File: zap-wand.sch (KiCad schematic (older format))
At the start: 14 parts

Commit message: Various bits
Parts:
- removed C?: 100u, symbol C
- removed Q? (x2): Q_NPN_EBC, symbol Q_NPN_EBC
- removed Q?: Q_NMOS_GDS, symbol Q_NMOS_GDS
- removed R?: 510R, symbol R
- removed R? (x2): 1k, symbol R
- removed R?: 100k, symbol R
- removed SW_PWR: SWITCH_SPST, symbol SWITCH_SPST
- added C2: 47u, agg:0805, symbol C
- added C3, C4: 1u, agg:0805, symbol C_Small
- added IC1: NC7WZ02, agg-dev:US8-3.1mm, symbol NC7WZ02
- added Q1: Q_PMOS_GDS, agg:SOT-323, symbol Q_PMOS_GDS
- added R1: 1k, agg:0805, symbol R
- added R2: 100k, agg:0805, symbol R
- added RV1: 100k, parts:PVZ2A, symbol POT
- added U1: NCP103, parts:UDFN4, symbol NCP103
- BATT1: renamed from BATT; footprint (none) -> agg:SM02B-PASS
- C1: renamed from C?; footprint (none) -> agg:0805; Farnell (none) -> 2497051
- D1: renamed from D?; footprint (none) -> LEDs:LED-5MM
- R3: renamed from R?; value 1k -> 100R; footprint (none) -> agg:0805; Farnell (none) -> 2447552
- SW1: renamed from SW?; footprint (none) -> parts:FSM10JH; Farnell (none) -> 1555986
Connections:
- net labels added: +3V3, GND
- wire segments 13 -> 17
- no-connect marks 0 -> 1

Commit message: Various tweaks and fixes
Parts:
- removed RV1: 100k, parts:PVZ2A, symbol POT
- added R4: 10k, agg:0603, symbol R
- added R5: 18k, agg:0603, symbol R
- BATT1: footprint agg:SM02B-PASS -> agg:SIL-254P-02
- C1: footprint agg:0805 -> agg:0603; Farnell 2497051 -> 2494233
- C2: value 47u -> 10n; Farnell 2362109 -> 2470490
- C3, C4: footprint agg:0805 -> agg:0603; Farnell 2496995 -> 2362099
- D1: footprint LEDs:LED-5MM -> agg:SIL-254P-02
- R1: footprint agg:0805 -> agg:0603; Farnell 2447473 -> 9330380
- R2: value 100k -> 820k; footprint agg:0805 -> agg:0603; Farnell 2447551 -> 9331581
- R3: footprint agg:0805 -> agg:0603; Farnell 2447552 -> 2447227
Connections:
- net +3V3: now also R5.1; no longer R2.1
- net GND: now also R4.1
- net at C1.2, SW1.2: now also R4.2
- net at C2.1, IC1.5 (A2), IC1.6 (B2): now also R2.2
- new net: R2.1, R5.2
- no-connect marks 1 -> 0
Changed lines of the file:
@@
 F 0 "BATT1" H 1218 2075 50  0001 L CNN
 F 1 "Battery" H 1218 2030 50  0001 L CNN
-F 2 "agg:SM02B-PASS" V 1100 2115 50  0001 C CNN
+F 2 "agg:SIL-254P-02" V 1100 2115 50  0001 C CNN
 F 3 "" V 1100 2115 50  0000 C CNN
 	1    1100 2075
@@
 F 0 "D1" H 5096 2442 50  0001 R CNN
 F 1 "LED" V 5050 2442 50  0001 R CNN
-F 2 "LEDs:LED-5MM" H 5050 2550 50  0001 C CNN
+F 2 "agg:SIL-254P-02" H 5050 2550 50  0001 C CNN
 F 3 "" H 5050 2550 50  0000 C CNN
 	1    5050 2550
@@
 F 0 "R3" H 4980 2154 50  0001 R CNN
 F 1 "100R" V 5050 2200 50  0000 C CNN
-F 2 "agg:0805" V 4980 2200 50  0001 C CNN
-F 3 "http://www.farnell.com/datasheets/1849611.pdf?_ga=1.16398518.1253160071.1453215511" H 5050 2200 50  0001 C CNN
-F 4 "2447552" H 5050 2200 60  0001 C CNN "Farnell"
+F 2 "agg:0603" V 4980 2200 50  0001 C CNN
+F 3 "http://www.farnell.com/datasheets/1849611.pdf?_ga=1.214886046.860814275.1465901405" H 5050 2200 50  0001 C CNN
+F 4 "2447227" H 5050 2200 60  0001 C CNN "Farnell"
 	1    5050 2200
 	-1   0    0    1
@@
 F 0 "C1" V 2873 1800 50  0001 C CNN
 F 1 "10u" V 2965 1800 50  0000 C CNN
-F 2 "agg:0805" H 3163 1650 50  0001 C CNN
-F 3 "http://www.farnell.com/datasheets/1958513.pdf?_ga=1.212596244.1253160071.1453215511" H 3125 1800 50  0001 C CNN
-F 4 "2497051" H 3125 1800 60  0001 C CNN "Farnell"
+F 2 "agg:0603" H 3163 1650 50  0001 C CNN
+F 3 "http://www.farnell.com/datasheets/1955682.pdf?_ga=1.157737651.860814275.1465901405" H 3125 1800 50  0001 C CNN
+F 4 "2494233" H 3125 1800 60  0001 C CNN "Farnell"
 	1    3125 1800
 	0    1    1    0
@@
 P 4025 1850
 F 0 "C2" V 3773 1850 50  0001 C CNN
-F 1 "47u" V 3865 1850 50  0000 C CNN
+F 1 "10n" V 3865 1850 50  0000 C CNN
 F 2 "agg:0805" H 4063 1700 50  0001 C CNN
-F 3 "http://www.farnell.com/datasheets/2047835.pdf" H 4025 1850 50  0001 C CNN
-F 4 "2362109" H 4025 1850 60  0001 C CNN "Farnell"
+F 3 "http://www.farnell.com/datasheets/1889704.pdf?_ga=1.190770722.860814275.1465901405" H 4025 1850 50  0001 C CNN
+F 4 "2470490" H 4025 1850 60  0001 C CNN "Farnell"
 	1    4025 1850
 	0    1    1    0
@@
 F 0 "R1" H 3205 1904 50  0001 R CNN
 F 1 "1k" V 3275 1950 50  0000 C CNN
-F 2 "agg:0805" V 3205 1950 50  0001 C CNN
-F 3 "http://www.farnell.com/datasheets/1849611.pdf?_ga=1.167509182.1253160071.1453215511" H 3275 1950 50  0001 C CNN
-F 4 "2447473" H 3275 1950 60  0001 C CNN "Farnell"
+F 2 "agg:0603" V 3205 1950 50  0001 C CNN
+F 3 "http://www.farnell.com/datasheets/1788326.pdf?_ga=1.214886046.860814275.1465901405" H 3275 1950 50  0001 C CNN
+F 4 "9330380" H 3275 1950 60  0001 C CNN "Farnell"
 	1    3275 1950
 	-1   0    0    1
@@
 Connection ~ 4750 1850
 $Comp
-L GND #PWR09
+L GND #PWR05
 U 1 1 578BBB74
 P 2200 2250
-F 0 "#PWR09" H 2200 2000 50  0001 C CNN
+F 0 "#PWR05" H 2200 2000 50  0001 C CNN
 F 1 "GND" H 2325 2175 50  0001 C CNN
 F 2 "" H 2200 2250 50  0000 C CNN
@@
 	1    0    0    -1
 $EndComp
-$Comp
-L POT RV1
-U 1 1 578BD570
-P 4175 1600
-F 0 "RV1" H 4175 1386 50  0001 C CNN
-F 1 "100k" H 4175 1600 50  0000 C CNN
-F 2 "parts:PVZ2A" H 4175 1600 50  0001 C CNN
-F 3 "http://www.farnell.com/datasheets/477473.pdf?_ga=1.242785154.1253160071.1453215511" H 4175 1600 50  0001 C CNN
-F 4 "1771728" H 4175 1600 60  0001 C CNN "Farnell"
-	1    4175 1600
-	1    0    0    1
-$EndComp
 Wire Wire Line
 	4175 1850 4175 1750
-NoConn ~ 4325 1600
 $Comp
 L R R2
 U 1 1 578BDA2A
-P 3875 1600
-F 0 "R2" H 3805 1554 50  0001 R CNN
-F 1 "100k" V 3875 1600 50  0000 C CNN
-F 2 "agg:0805" V 3805 1600 50  0001 C CNN
-F 3 "http://www.farnell.com/datasheets/1849611.pdf?_ga=1.167509182.1253160071.1453215511" H 3875 1600 50  0001 C CNN
-F 4 "2447551" H 3875 1600 60  0001 C CNN "Farnell"
-	1    3875 1600
-	0    -1   -1   0
+P 4175 1600
+F 0 "R2" H 4105 1554 50  0001 R CNN
+F 1 "820k" V 4175 1600 50  0000 C CNN
+F 2 "agg:0603" V 4105 1600 50  0001 C CNN
+F 3 "http://www.farnell.com/datasheets/1788326.pdf?_ga=1.148300478.860814275.1465901405" H 4175 1600 50  0001 C CNN
+F 4 "9331581" H 4175 1600 60  0001 C CNN "Farnell"
+	1    4175 1600
+	1    0    0    -1
 $EndComp
 $Comp
@@
 	1100 2250 2200 2250
 Connection ~ 1400 2100
-$Comp
-L C_Small C4
-U 1 1 578C05A9
-P 2200 2100
-F 0 "C4" H 2292 2146 50  0001 L CNN
-F 1 "1u" H 2300 2100 50  0000 L CNN
-F 2 "agg:0805" H 2200 2100 50  0001 C CNN
-F 3 "http://www.farnell.com/datasheets/1958513.pdf?_ga=1.205166480.1253160071.1453215511" H 2200 2100 50  0001 C CNN
-F 4 "2496995" H 2200 2100 60  0001 C CNN "Farnell"
-	1    2200 2100
-	1    0    0    -1
-$EndComp
 Connection ~ 1400 2250
 Wire Wire Line
@@
 P 1400 2000
 F 0 "C3" H 1492 2046 50  0001 L CNN
-F 1 "1u" H 1250 2000 50  0000 L CNN
-F 2 "agg:0805" H 1400 2000 50  0001 C CNN
-F 3 "http://www.farnell.com/datasheets/1958513.pdf?_ga=1.205166480.1253160071.1453215511" H 1400 2000 50  0001 C CNN
-F 4 "2496995" H 1400 2000 60  0001 C CNN "Farnell"
+F 1 "1u" H 1475 2000 50  0000 L CNN
+F 2 "agg:0603" H 1400 2000 50  0001 C CNN
+F 3 "http://www.farnell.com/datasheets/2047881.pdf?_ga=1.124134275.860814275.1465901405" H 1400 2000 50  0001 C CNN
+F 4 "2362099" H 1400 2000 60  0001 C CNN "Farnell"
 	1    1400 2000
 	1    0    0    -1
 $EndComp
 $Comp
-L +3V3 #PWR?
+L +3V3 #PWR06
 U 1 1 578CFCA7
 P 2200 2000
-F 0 "#PWR?" H 2200 1850 50  0001 C CNN
+F 0 "#PWR06" H 2200 1850 50  0001 C CNN
 F 1 "+3V3" H 2215 2173 50  0000 C CNN
 F 2 "" H 2200 2000 50  0000 C CNN
@@
 $EndComp
 $Comp
-L +3V3 #PWR?
+L +3V3 #PWR07
 U 1 1 578CFCC6
 P 2775 1600
-F 0 "#PWR?" H 2775 1450 50  0001 C CNN
+F 0 "#PWR07" H 2775 1450 50  0001 C CNN
 F 1 "+3V3" H 2790 1773 50  0000 C CNN
 F 2 "" H 2775 1600 50  0000 C CNN
@@
 $EndComp
 $Comp
-L +3V3 #PWR?
+L +3V3 #PWR08
 U 1 1 578CFCE3
 P 3575 1650
-F 0 "#PWR?" H 3575 1500 50  0001 C CNN
+F 0 "#PWR08" H 3575 1500 50  0001 C CNN
 F 1 "+3V3" H 3590 1823 50  0000 C CNN
 F 2 "" H 3575 1650 50  0000 C CNN
@@
 $EndComp
 $Comp
-L +3V3 #PWR?
+L +3V3 #PWR09
 U 1 1 578CFCF1
-P 3725 1600
-F 0 "#PWR?" H 3725 1450 50  0001 C CNN
-F 1 "+3V3" H 3800 1725 50  0000 C CNN
-F 2 "" H 3725 1600 50  0000 C CNN
-F 3 "" H 3725 1600 50  0000 C CNN
-	1    3725 1600
-	1    0    0    -1
-$EndComp
-$Comp
-L +3V3 #PWR?
+P 4175 1150
+F 0 "#PWR09" H 4175 1000 50  0001 C CNN
+F 1 "+3V3" H 4250 1275 50  0000 C CNN
+F 2 "" H 4175 1150 50  0000 C CNN
+F 3 "" H 4175 1150 50  0000 C CNN
+	1    4175 1150
+	1    0    0    -1
+$EndComp
+$Comp
+L +3V3 #PWR010
 U 1 1 578CFCFF
 P 4450 1650
-F 0 "#PWR?" H 4450 1500 50  0001 C CNN
+F 0 "#PWR010" H 4450 1500 50  0001 C CNN
 F 1 "+3V3" H 4465 1823 50  0000 C CNN
 F 2 "" H 4450 1650 50  0000 C CNN
@@
 $EndComp
 $Comp
-L +3V3 #PWR?
+L +3V3 #PWR011
 U 1 1 578CFD0D
 P 5050 1650
-F 0 "#PWR?" H 5050 1500 50  0001 C CNN
+F 0 "#PWR011" H 5050 1500 50  0001 C CNN
 F 1 "+3V3" H 5065 1823 50  0000 C CNN
 F 2 "" H 5050 1650 50  0000 C CNN
@@
 	1    0    0    -1
 $EndComp
+$Comp
+L R R4
+U 1 1 578E3B6A
+P 2975 1950
+F 0 "R4" H 2905 1904 50  0001 R CNN
+F 1 "10k" V 2975 1950 50  0000 C CNN
+F 2 "agg:0603" V 2905 1950 50  0001 C CNN
+F 3 "http://www.farnell.com/datasheets/1788326.pdf?_ga=1.190834594.860814275.1465901405" H 2975 1950 50  0001 C CNN
+F 4 "9330399" H 2975 1950 60  0001 C CNN "Farnell"
+	1    2975 1950
+	-1   0    0    1
+$EndComp
+Connection ~ 2975 1800
+$Comp
+L GND #PWR012
+U 1 1 578E3BBA
+P 2975 2100
+F 0 "#PWR012" H 2975 1850 50  0001 C CNN
+F 1 "GND" H 3100 2025 50  0001 C CNN
+F 2 "" H 2975 2100 50  0000 C CNN
+F 3 "" H 2975 2100 50  0000 C CNN
+	1    2975 2100
+	1    0    0    -1
+$EndComp
+$Comp
+L R R5
+U 1 1 578E56B2
+P 4175 1300
+F 0 "R5" H 4105 1254 50  0001 R CNN
+F 1 "18k" V 4175 1300 50  0000 C CNN
+F 2 "agg:0603" V 4105 1300 50  0001 C CNN
+F 3 "http://www.farnell.com/datasheets/1788326.pdf?_ga=1.190834594.860814275.1465901405" H 4175 1300 50  0001 C CNN
+F 4 "9330720" H 4175 1300 60  0001 C CNN "Farnell"
+	1    4175 1300
+	1    0    0    -1
+$EndComp
+$Comp
+L C_Small C4
+U 1 1 578E5A07
+P 2200 2100
+F 0 "C4" H 2292 2146 50  0001 L CNN
+F 1 "1u" H 2275 2100 50  0000 L CNN
+F 2 "agg:0603" H 2200 2100 50  0001 C CNN
+F 3 "http://www.farnell.com/datasheets/2047881.pdf?_ga=1.124134275.860814275.1465901405" H 2200 2100 50  0001 C CNN
+F 4 "2362099" H 2200 2100 60  0001 C CNN "Farnell"
+	1    2200 2100
+	1    0    0    -1
+$EndComp

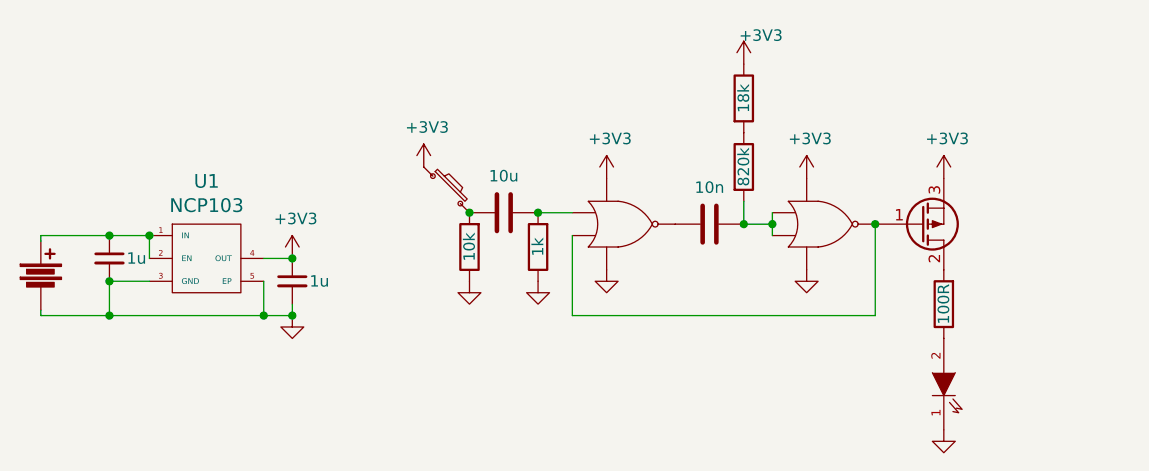
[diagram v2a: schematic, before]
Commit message: Beefier regulator, pcb shuffle
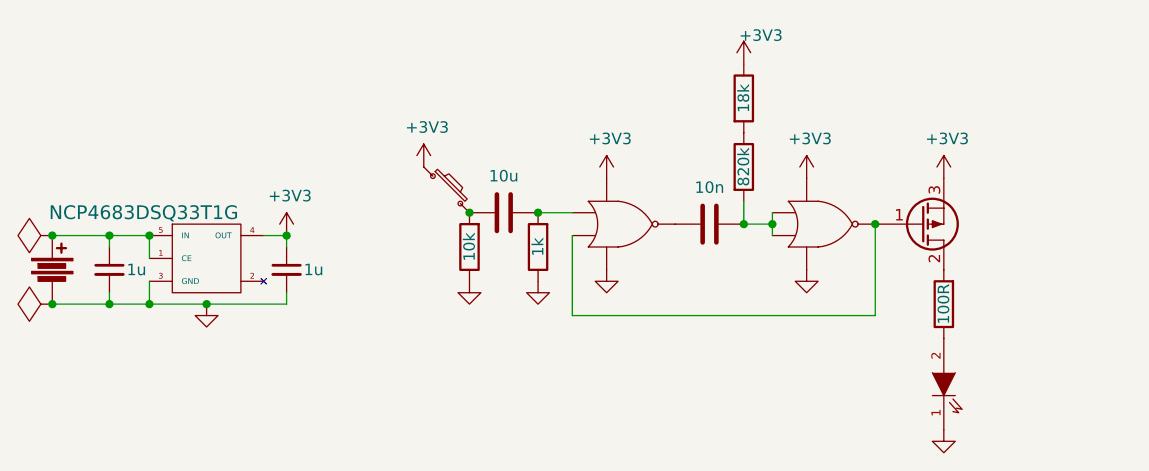
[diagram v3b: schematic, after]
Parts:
- removed U1: NCP103, parts:UDFN4, symbol NCP103
- added U1: NCP4683DSQ33T1G, agg:SC-70-5, symbol NCP4683DSQxxT1G
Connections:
- net +3V3: now also U1.4 (OUT)
- net GND: now also U1.3 (GND)
- net at BATT1.1, C3.1: now also U1.1 (CE), U1.5 (IN)
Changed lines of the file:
@@
 LIBS:nc7wz02
 LIBS:ncp103
+LIBS:ncp4683dsqxxt1g
 LIBS:zap-wand-cache
 EELAYER 25 0
@@
 L Battery BATT1
 U 1 1 578B9B48
-P 1100 2075
-F 0 "BATT1" H 1218 2075 50  0001 L CNN
-F 1 "Battery" H 1218 2030 50  0001 L CNN
-F 2 "agg:SIL-254P-02" V 1100 2115 50  0001 C CNN
-F 3 "" V 1100 2115 50  0000 C CNN
-	1    1100 2075
+P 1150 2050
+F 0 "BATT1" H 1268 2050 50  0001 L CNN
+F 1 "Battery" H 1268 2005 50  0001 L CNN
+F 2 "agg:SIL-254P-02" V 1150 2090 50  0001 C CNN
+F 3 "" V 1150 2090 50  0000 C CNN
+	1    1150 2050
 	1    0    0    -1
 $EndComp
@@
 L GND #PWR05
 U 1 1 578BBB74
-P 2200 2250
-F 0 "#PWR05" H 2200 2000 50  0001 C CNN
-F 1 "GND" H 2325 2175 50  0001 C CNN
-F 2 "" H 2200 2250 50  0000 C CNN
-F 3 "" H 2200 2250 50  0000 C CNN
-	1    2200 2250
+P 1825 2200
+F 0 "#PWR05" H 1825 1950 50  0001 C CNN
+F 1 "GND" H 1950 2125 50  0001 C CNN
+F 2 "" H 1825 2200 50  0000 C CNN
+F 3 "" H 1825 2200 50  0000 C CNN
+	1    1825 2200
 	1    0    0    -1
 $EndComp
@@
 $EndComp
 $Comp
-L NCP103 U1
-U 1 1 578C0311
-P 1825 2000
-F 0 "U1" H 1825 2337 60  0000 C CNN
-F 1 "NCP103" H 1825 2231 60  0000 C CNN
-F 2 "parts:UDFN4" H 1825 2000 60  0001 C CNN
-F 3 "http://www.farnell.com/datasheets/1825943.pdf" H 1825 2000 60  0001 C CNN
-F 4 "2454538" H 1825 2000 60  0001 C CNN "Farnell"
-	1    1825 2000
-	1    0    0    -1
-$EndComp
-Wire Wire Line
-	1575 2100 1400 2100
-Wire Wire Line
-	1100 1900 1575 1900
-Connection ~ 1400 1900
-Wire Wire Line
-	1400 2100 1400 2250
-Wire Wire Line
-	1100 2250 2200 2250
-Connection ~ 1400 2100
-Connection ~ 1400 2250
-Wire Wire Line
-	2200 2250 2200 2200
-Connection ~ 2200 2250
-Wire Wire Line
-	2075 2100 2075 2250
-Connection ~ 2075 2250
-Wire Wire Line
-	2075 2000 2200 2000
-Connection ~ 2200 2000
-Wire Wire Line
-	1100 2250 1100 2225
-Wire Wire Line
-	1100 1925 1100 1900
-Wire Wire Line
-	1575 1900 1575 2000
-Connection ~ 1575 1900
-$Comp
 L C_Small C3
 U 1 1 578C1086
-P 1400 2000
-F 0 "C3" H 1492 2046 50  0001 L CNN
-F 1 "1u" H 1475 2000 50  0000 L CNN
-F 2 "agg:0603" H 1400 2000 50  0001 C CNN
-F 3 "http://www.farnell.com/datasheets/2047881.pdf?_ga=1.124134275.860814275.1465901405" H 1400 2000 50  0001 C CNN
-F 4 "2362099" H 1400 2000 60  0001 C CNN "Farnell"
-	1    1400 2000
+P 1400 2050
+F 0 "C3" H 1492 2096 50  0001 L CNN
+F 1 "1u" H 1475 2050 50  0000 L CNN
+F 2 "agg:0603" H 1400 2050 50  0001 C CNN
+F 3 "http://www.farnell.com/datasheets/2047881.pdf?_ga=1.124134275.860814275.1465901405" H 1400 2050 50  0001 C CNN
+F 4 "2362099" H 1400 2050 60  0001 C CNN "Farnell"
+	1    1400 2050
 	1    0    0    -1
 $EndComp
@@
 L +3V3 #PWR06
 U 1 1 578CFCA7
-P 2200 2000
-F 0 "#PWR06" H 2200 1850 50  0001 C CNN
-F 1 "+3V3" H 2215 2173 50  0000 C CNN
-F 2 "" H 2200 2000 50  0000 C CNN
-F 3 "" H 2200 2000 50  0000 C CNN
-	1    2200 2000
+P 2175 1900
+F 0 "#PWR06" H 2175 1750 50  0001 C CNN
+F 1 "+3V3" H 2190 2073 50  0000 C CNN
+F 2 "" H 2175 1900 50  0000 C CNN
+F 3 "" H 2175 1900 50  0000 C CNN
+	1    2175 1900
 	1    0    0    -1
 $EndComp
@@
 $EndComp
 $Comp
+L NCP4683DSQxxT1G U1
+U 1 1 5790C603
+P 1825 2000
+F 0 "U1" H 1875 2000 60  0001 C CNN
+F 1 "NCP4683DSQ33T1G" H 1550 2200 60  0000 C CNN
+F 2 "agg:SC-70-5" H 1725 1650 60  0001 C CNN
+F 3 "http://www.farnell.com/datasheets/1878398.pdf" H 1825 1750 60  0001 C CNN
+F 4 "2464280" H 1825 2000 60  0001 C CNN "Farnell"
+	1    1825 2000
+	1    0    0    -1
+$EndComp
+$Comp
 L C_Small C4
 U 1 1 578E5A07
-P 2200 2100
-F 0 "C4" H 2292 2146 50  0001 L CNN
-F 1 "1u" H 2275 2100 50  0000 L CNN
-F 2 "agg:0603" H 2200 2100 50  0001 C CNN
-F 3 "http://www.farnell.com/datasheets/2047881.pdf?_ga=1.124134275.860814275.1465901405" H 2200 2100 50  0001 C CNN
-F 4 "2362099" H 2200 2100 60  0001 C CNN "Farnell"
-	1    2200 2100
-	1    0    0    -1
-$EndComp
+P 2175 2050
+F 0 "C4" H 2267 2096 50  0001 L CNN
+F 1 "1u" H 2250 2050 50  0000 L CNN
+F 2 "agg:0603" H 2175 2050 50  0001 C CNN
+F 3 "http://www.farnell.com/datasheets/2047881.pdf?_ga=1.124134275.860814275.1465901405" H 2175 2050 50  0001 C CNN
+F 4 "2362099" H 2175 2050 60  0001 C CNN "Farnell"
+	1    2175 2050
+	1    0    0    -1
+$EndComp
+Wire Wire Line
+	1150 2200 2175 2200
+Wire Wire Line
+	2175 2200 2175 2150
+Wire Wire Line
+	1150 1900 1575 1900
+Wire Wire Line
+	2075 1900 2175 1900
+Wire Wire Line
+	2175 1900 2175 1950
+Connection ~ 2175 1900
+Connection ~ 1825 2200
+Wire Wire Line
+	1400 2150 1400 2200
+Connection ~ 1400 2200
+Wire Wire Line
+	1400 1950 1400 1900
+Connection ~ 1400 1900
+Wire Wire Line
+	1575 1900 1575 2000
+Connection ~ 1575 1900
+Wire Wire Line
+	1575 2100 1575 2200
+Connection ~ 1575 2200
+$Comp
+L PWR_FLAG #FLG013
+U 1 1 5790C912
+P 1150 1900
+F 0 "#FLG013" H 1150 1995 50  0001 C CNN
+F 1 "PWR_FLAG" V 1150 2078 50  0001 L CNN
+F 2 "" H 1150 1900 50  0000 C CNN
+F 3 "" H 1150 1900 50  0000 C CNN
+	1    1150 1900
+	0    -1   -1   0
+$EndComp
+$Comp
+L PWR_FLAG #FLG014
+U 1 1 5790C924
+P 1150 2200
+F 0 "#FLG014" H 1150 2295 50  0001 C CNN
+F 1 "PWR_FLAG" V 1150 2378 50  0001 L CNN
+F 2 "" H 1150 2200 50  0000 C CNN
+F 3 "" H 1150 2200 50  0000 C CNN
+	1    1150 2200
+	0    -1   -1   0
+$EndComp
+Connection ~ 1150 1900
+Connection ~ 1150 2200
 $EndSCHEMATC
